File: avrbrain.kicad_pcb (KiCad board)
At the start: 4 copper layers, 85 x 56 mm, 63 parts, among them J1 UPDI, J10 PORTG, J11 UEXT, J12 SM04B-SRSS-TB, J2 PORTA, J3 PORTB, J4 PORTC, J5 PORTD, J6 PORTE, J7 PORTF, J8 XKTF-0803-0, J9 U254-051T-4BH81-S2S, Q1 BSS138, SW1 RESET, SW3 PROG_EN, U1 AVR128DB64x-xPT, U2 AMS1117-3.3, U3 CH340C, U4 PCF8563T, Y1 32kHz

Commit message: Add silkscreen pinouts
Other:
- board text added: "5V"
- board text added: "AVRbrain (C)2025 J.B. Langston github.com/jblang/avrbrain"
- board text added: "NC"
- board text added: "PA0"
- board text added: "PA1"
- board text added: "PA2"
- board text added: "PA3"
- board text added: "PA4"
- board text added: "PA5"
- board text added: "PA6"
- board text added: "PA7"
- board text added: "PB0"
- board text added: "PB1"
- board text added: "PB2"
- board text added: "PB3"
- board text added: "PB4"
- board text added: "PB5"
- board text added: "PB6"
- board text added: "PB7"
- board text added: "PC0"
- board text added: "PC1"
- board text added: "PC2"
- board text added: "PC3"
- board text added: "PC4"
- board text added: "PC5"
- board text added: "PC6"
- board text added: "PC7"
- board text added: "PD0"
- board text added: "PD1"
- board text added: "PD2"
- board text added: "PD3"
- board text added: "PD4"
- board text added: "PD5"
- board text added: "PD6"
- board text added: "PD7"
- board text added: "PE0"
- board text added: "PE1"
- board text added: "PE2"
- board text added: "PE3"
- board text added: "PE4"
- board text added: "PE5"
- board text added: "PE6"
- board text added: "PE7"
- board text added: "PF0"
- board text added: "PF1"
- board text added: "PF2"
- board text added: "PF3"
- board text added: "PF4"
- board text added: "PF5"
- board text added: "PG0"
- board text added: "PG1"
- board text added: "PG2"
- board text added: "PG3"
- board text added: "PG4"
- board text added: "PG5"
- board text added: "PG6"
- board text added: "PG7"
- board text removed: "Copyright (C)2024 J.B. Langston https://github.com/jblang/avrbrain"

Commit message: Final (?!) tweaks
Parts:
- added C19: 1uf, Capacitor_SMD:C_1206_3216Metric, F.Cu at (173.8, 110.0)
- moved D2 2.51 mm to (175.1, 85.3)
- moved J11 0.77 mm to (193.7, 94.4)
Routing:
- net +3.3V: track 11.3 -> 4.67 mm, vias 3 -> 0
- net /PB7: track 43.5 -> 48.1 mm
- net /PB6: track 45.2 -> 49.6 mm
- net /PB5: track 40.9 -> 45.0 mm
- net /PB4: track 42.7 -> 46.5 mm
- net /PB3: track 38.3 -> 41.9 mm
- net /PB2: track 39.9 -> 43.3 mm
- net /PB1: track 35.3 -> 38.4 mm
- net /PB0: track 36.4 -> 39.2 mm
- net Net-(JP1-A): track 21.9 -> 24.6 mm
- net TXC: track 33.9 -> 36.6 mm
- net Net-(D2-K): track 11.3 -> 8.75 mm
- net +5V: track 21.2 -> 23.6 mm
- net GND: track 46.7 -> 49.1 mm
- net /PD7: track 33.8 -> 35.7 mm, vias 0 -> 2
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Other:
- board text added: "UEXT"

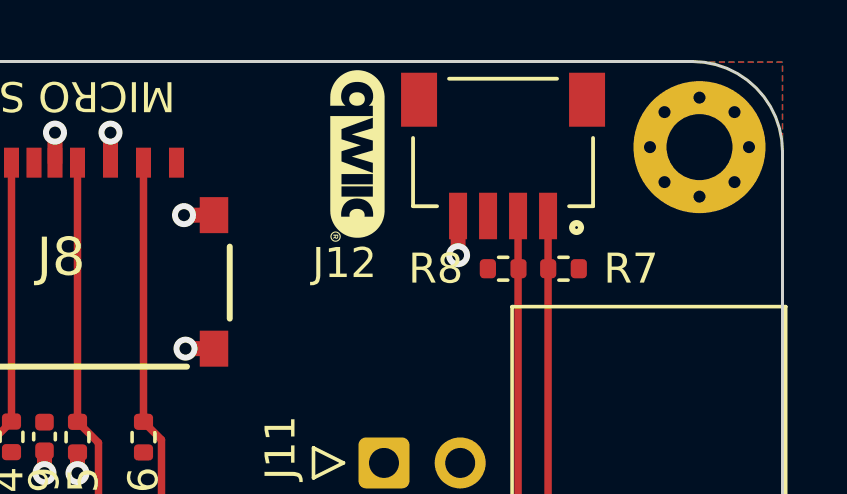
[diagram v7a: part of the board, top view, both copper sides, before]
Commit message: Add custom symbols and footprints
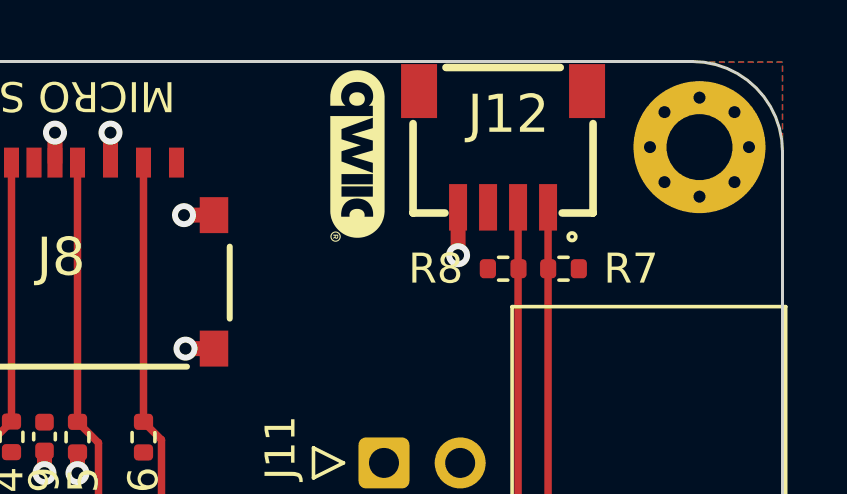
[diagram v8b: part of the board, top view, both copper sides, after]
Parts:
- J12: footprint Custom:JST_SM04B-SRSS-TB_LF__SN_ -> SamacSys_Parts:SM04B-SRSS-TB_LFSN_
- moved J12 5.79 mm to (200.7, 81.2)
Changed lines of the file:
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@@
 	(net 93 "+5V")
 	(net 94 "unconnected-(J7-Pin_8-Pad8)")
-	(footprint "Custom:JST_SM04B-SRSS-TB_LF__SN_"
+	(footprint "SamacSys_Parts:SM04B-SRSS-TB_LFSN_"
 		(layer "F.Cu")
-		(at 197.685476 86.127954 180)
+		(at 200.685476 81.179 180)
+		(descr "SM04B-SRSS-TB(LFSN)")
+		(tags "Connector")
 		(property "Reference" "J12"
-			(at 5.285476 -1.572046 0)
+			(at 2.822 -1.556 180)
 			(layer "F.SilkS")
 			(effects
 				(font
-					(size 1.001173 1.001173)
-					(thickness 0.15)
+					(size 1.27 1.27)
+					(thickness 0.254)
 				)
 			)
 		)
 		(property "Value" "SM04B-SRSS-TB"
-			(at 12.17039 5.74055 0)
-			(layer "F.Fab")
+			(at 2.822 -1.556 180)
+			(layer "F.SilkS")
+			(hide yes)
 			(effects
 				(font
-					(size 1.000567 1.000567)
-					(thickness 0.15)
+					(size 1.27 1.27)
+					(thickness 0.254)
 				)
 			)
 		)
-		(property "Footprint" "Custom:JST_SM04B-SRSS-TB_LF__SN_"
+		(property "Footprint" "SamacSys_Parts:SM04B-SRSS-TB_LFSN_"
 			(at 0 0 180)
-			(unlocked yes)
 			(layer "F.Fab")
 			(hide yes)
@@
 		(property "Datasheet" "https://www.jst-mfg.com/product/pdf/eng/eSH.pdf"
 			(at 0 0 180)
-			(unlocked yes)
 			(layer "F.Fab")
 			(hide yes)
@@
 		(property "Description" ""
 			(at 0 0 180)
-			(unlocked yes)
 			(layer "F.Fab")
 			(hide yes)
@@
 		(attr smd)
 		(fp_line
-			(start 3 0.325)
-			(end 3 2.6)
+			(start 6 -4.85)
+			(end 6 -1.87)
 			(stroke
-				(width 0.127)
+				(width 0.254)
 				(type solid)
 			)
@@
 		)
 		(fp_line
-			(start 2.2 0.325)
-			(end 3 0.325)
+			(start 6 -4.85)
+			(end 4.937 -4.85)
 			(stroke
-				(width 0.127)
+				(width 0.254)
 				(type solid)
 			)
@@
 		)
 		(fp_line
-			(start -1.8 4.575)
-			(end 1.8 4.575)
+			(start 1.094 0)
+			(end 4.903 0)
 			(stroke
-				(width 0.127)
+				(width 0.254)
 				(type solid)
 			)
@@
 		)
 		(fp_line
-			(start -2.2 0.325)
-			(end -3 0.325)
+			(start 0 -4.85)
+			(end 1.029 -4.85)
 			(stroke
-				(width 0.127)
+				(width 0.254)
 				(type solid)
 			)
@@
 		)
 		(fp_line
-			(start -3 0.325)
-			(end -3 2.6)
+			(start 0 -4.85)
+			(end 0 -1.87)
 			(stroke
-				(width 0.127)
+				(width 0.254)
 				(type solid)
 			)
@@
 		)
 		(fp_circle
-			(center -2.45 -0.385)
-			(end -2.35 -0.385)
+			(center 0.702 -5.642)
+			(end 0.702 -5.58163)
 			(stroke
-				(width 0.3)
+				(width 0.254)
 				(type solid)
 			)
@@
 		)
 		(fp_line
-			(start 3.65 5.025)
-			(end -3.65 5.025)
+			(start 6 0)
+			(end 0 0)
 			(stroke
-				(width 0.05)
-				(type solid)
-			)
-			(layer "F.CrtYd")
-		)
-		(fp_line
-			(start 3.65 -1.025)
-			(end 3.65 5.025)
-			(stroke
-				(width 0.05)
-				(type solid)
-			)
-			(layer "F.CrtYd")
-		)
-		(fp_line
-			(start -3.65 5.025)
-			(end -3.65 -1.025)
-			(stroke
-				(width 0.05)
-				(type solid)
-			)
-			(layer "F.CrtYd")
-		)
-		(fp_line
-			(start -3.65 -1.025)
-			(end 3.65 -1.025)
-			(stroke
-				(width 0.05)
-				(type solid)
-			)
-			(layer "F.CrtYd")
-		)
-		(fp_line
-			(start 3 4.575)
-			(end -3 4.575)
-			(stroke
-				(width 0.127)
+				(width 0.254)
 				(type solid)
 			)
@@
 		)
 		(fp_line
-			(start 3 0.325)
-			(end 3 4.575)
+			(start 6 -4.85)
+			(end 6 0)
 			(stroke
-				(width 0.127)
+				(width 0.254)
 				(type solid)
 			)
@@
 		)
 		(fp_line
-			(start -3 4.575)
-			(end -3 0.325)
+			(start 0 0)
+			(end 0 -4.85)
 			(stroke
-				(width 0.127)
+				(width 0.254)
 				(type solid)
 			)
@@
 		)
 		(fp_line
-			(start -3 0.325)
-			(end 3 0.325)
+			(start 0 -4.85)
+			(end 6 -4.85)
 			(stroke
-				(width 0.127)
+				(width 0.254)
 				(type solid)
 			)
 			(layer "F.Fab")
 		)
-		(fp_circle
-			(center -2.45 -0.385)
-			(end -2.35 -0.385)
-			(stroke
-				(width 0.3)
-				(type solid)
-			)
-			(fill none)
+		(fp_text user "${REFERENCE}"
+			(at 2.822 -1.556 180)
 			(layer "F.Fab")
+			(effects
+				(font
+					(size 1.27 1.27)
+					(thickness 0.254)
+				)
+			)
 		)
 		(pad "1" smd rect
-			(at -1.5 0 180)
+			(at 1.5 -4.661 180)
 			(size 0.6 1.55)
 			(layers "F.Cu" "F.Paste" "F.Mask")
@@
 			(pinfunction "Pin_1")
 			(pintype "passive")
-			(solder_mask_margin 0.102)
 		)
 		(pad "2" smd rect
-			(at -0.5 0 180)
+			(at 2.5 -4.661 180)
 			(size 0.6 1.55)
 			(layers "F.Cu" "F.Paste" "F.Mask")
@@
 			(pinfunction "Pin_2")
 			(pintype "passive")
-			(solder_mask_margin 0.102)
 		)
 		(pad "3" smd rect
-			(at 0.5 0 180)
+			(at 3.5 -4.661 180)
 			(size 0.6 1.55)
 			(layers "F.Cu" "F.Paste" "F.Mask")
@@
 			(pinfunction "Pin_3")
 			(pintype "passive")
-			(solder_mask_margin 0.102)
 		)
 		(pad "4" smd rect
-			(at 1.5 0 180)
+			(at 4.5 -4.661 180)
 			(size 0.6 1.55)
 			(layers "F.Cu" "F.Paste" "F.Mask")
@@
 			(pinfunction "Pin_4")
 			(pintype "passive")
-			(solder_mask_margin 0.102)
 		)
-		(pad "S1" smd rect
-			(at -2.8 3.875)
+		(pad "5" smd rect
+			(at 0.2 -0.786 180)
 			(size 1.2 1.8)
 			(layers "F.Cu" "F.Paste" "F.Mask")
-			(solder_mask_margin 0.102)
 		)
-		(pad "S2" smd rect
-			(at 2.8 3.875)
+		(pad "6" smd rect
+			(at 5.8 -0.786 180)
 			(size 1.2 1.8)
 			(layers "F.Cu" "F.Paste" "F.Mask")
-			(solder_mask_margin 0.102)
+		)
+		(model "SM04B-SRSS-TB_LF__SN_.stp"
+			(offset
+				(xyz 2.999999955 4.179999766 -0.2899999873)
+			)
+			(scale
+				(xyz 1 1 1)
+			)
+			(rotate
+				(xyz -90 0 0)
+			)
 		)
 	)
@@
 		(fp_arc
 			(start 7.25 4.1)
-			(mid 6.682004 5.496829)
+			(mid 6.682005 5.496831)
 			(end 5.3 6.1)
 			(stroke
@@
 		(fp_arc
 			(start 5.3 6.1)
-			(mid 4.714381 5.984481)
+			(mid 4.714387 5.984475)
 			(end 4.22 5.65)
 			(stroke
@@
 		(fp_arc
 			(start 6.6 4.1)
-			(mid 6.222443 5.037354)
+			(mid 6.222442 5.03735)
 			(end 5.3 5.45)
 			(stroke
